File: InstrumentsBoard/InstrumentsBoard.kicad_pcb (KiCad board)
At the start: 2 copper layers, 105.4 x 38.1 mm, 24 parts, among them J1 RJ45_LED_Shielded, Q1 BSS138, Q2 BSS138, U1 Teensy4.1_DEV-16771, U2 OKI

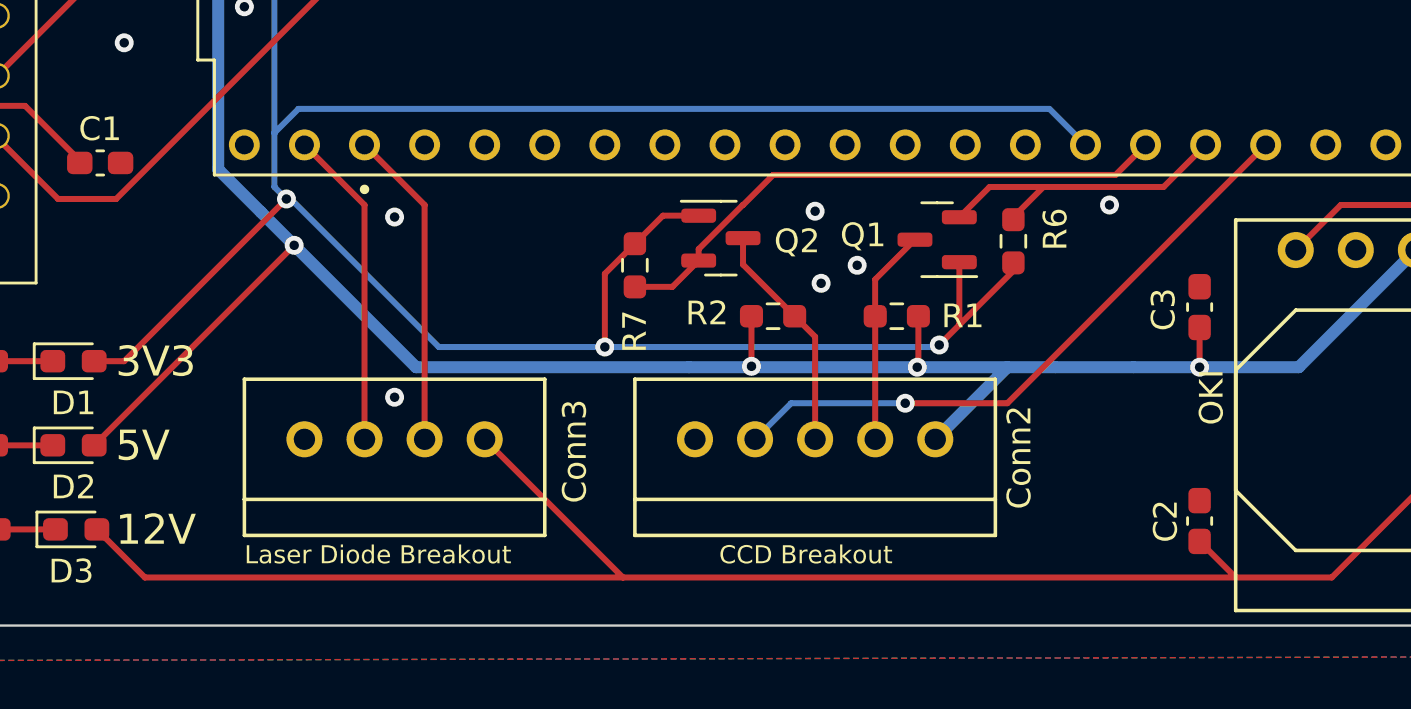
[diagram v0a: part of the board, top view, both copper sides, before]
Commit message: change pin ordering for ccd molex
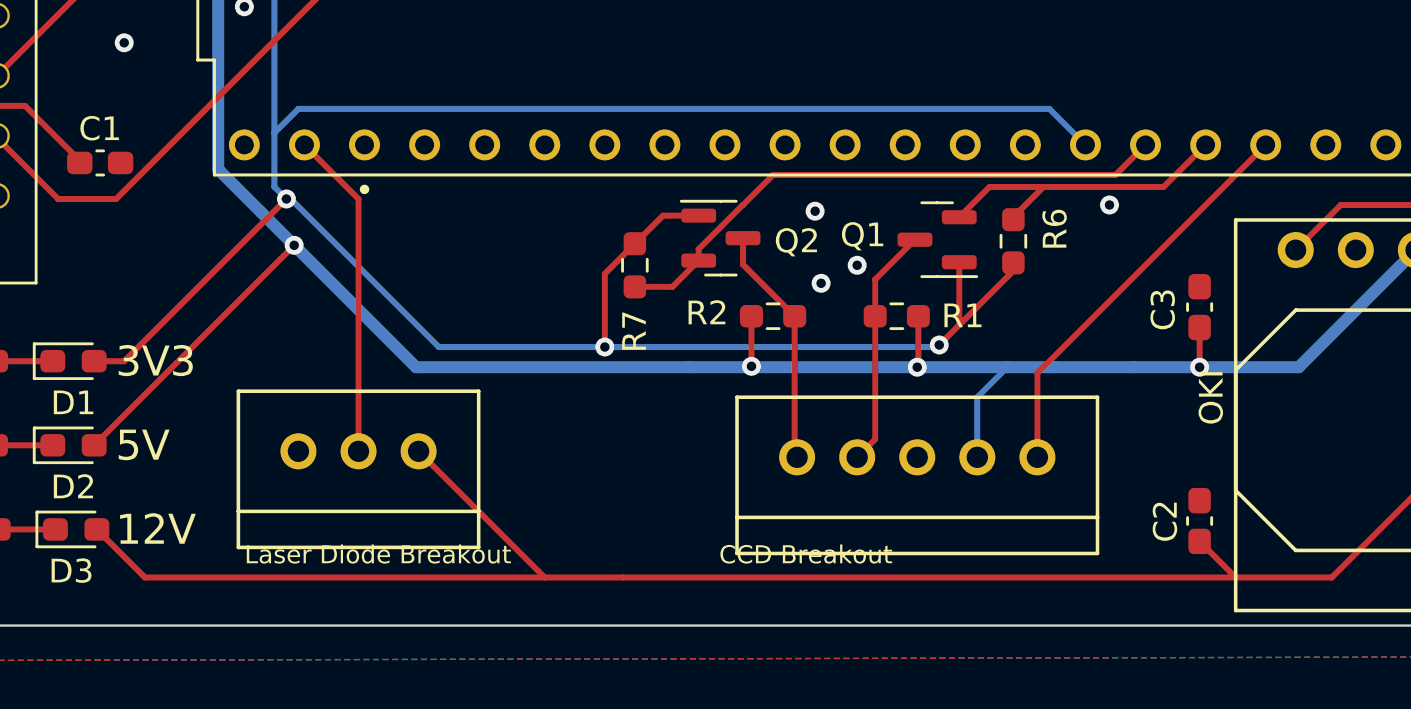
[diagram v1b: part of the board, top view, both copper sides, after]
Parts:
- Conn3: value Molex_SL_04 -> Molex_SL_03; footprint MRDT_Connectors:MOLEX_SL_04_Vertical -> MRDT_Connectors:MOLEX_SL_03_Vertical
- moved Conn2 4.38 mm to (86.4, 66.8)
- moved Conn3 2.84 mm to (60.2, 66.5)
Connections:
- Conn2 pad 1: +5V -> CCD_Vout
- Conn2 pad 2: CCD_CLK_5V -> +5V
- Conn2 pad 3: CCD_ROG_5V -> GND
- Conn2 pad 4: CCD_Vout -> CCD_CLK_5V
- Conn2 pad 5: GND -> CCD_ROG_5V
- Conn3 pad 2: Red_LED -> Green_LED
- Conn3 pad 3: Green_LED -> GND
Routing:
- net Red_LED: track 13.5 -> 0.00 mm
- net CCD_Vout: track 26.7 -> 17.2 mm, vias 1 -> 0
- net CCD_CLK_5V: track 9.14 -> 10.2 mm
- net +12V: track 95.5 -> 94.8 mm
- net GND: vias 9 -> 7

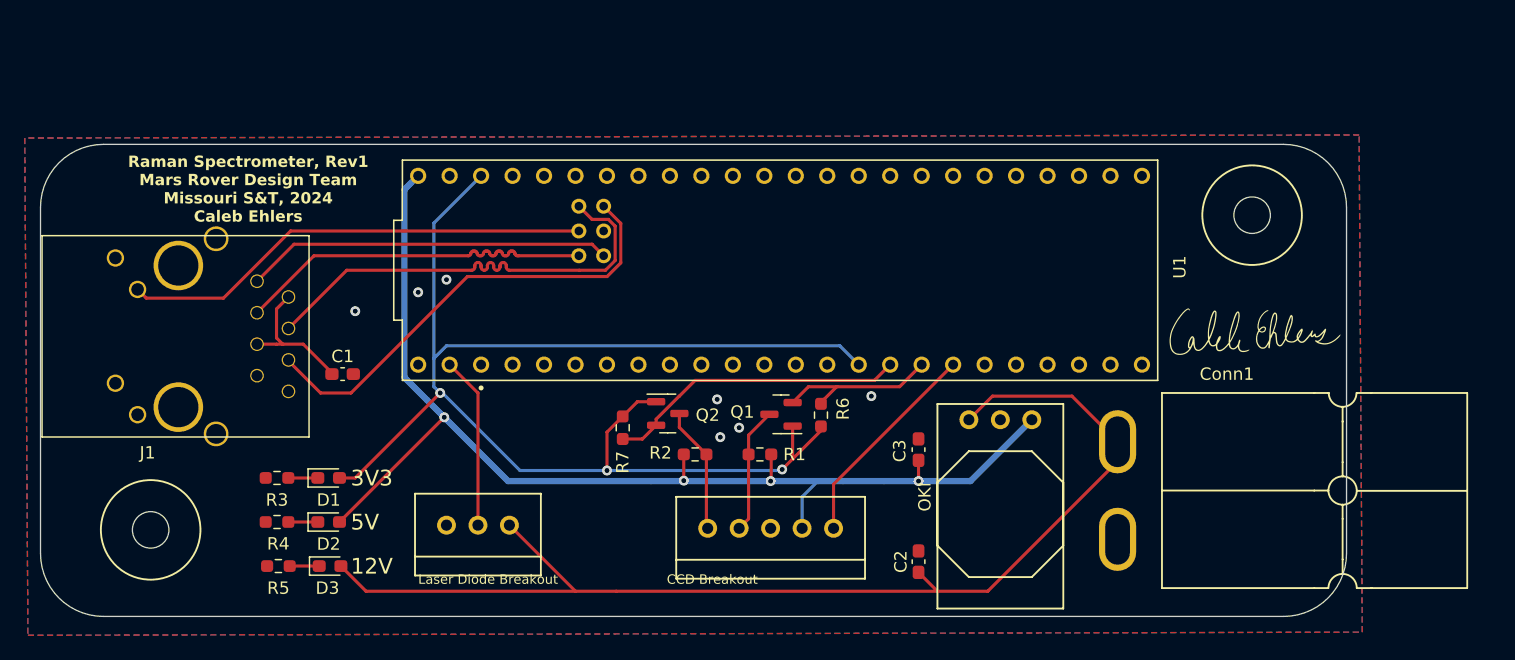
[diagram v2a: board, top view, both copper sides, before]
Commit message: Added Hamamatsu Connector, Updated Silkscreen
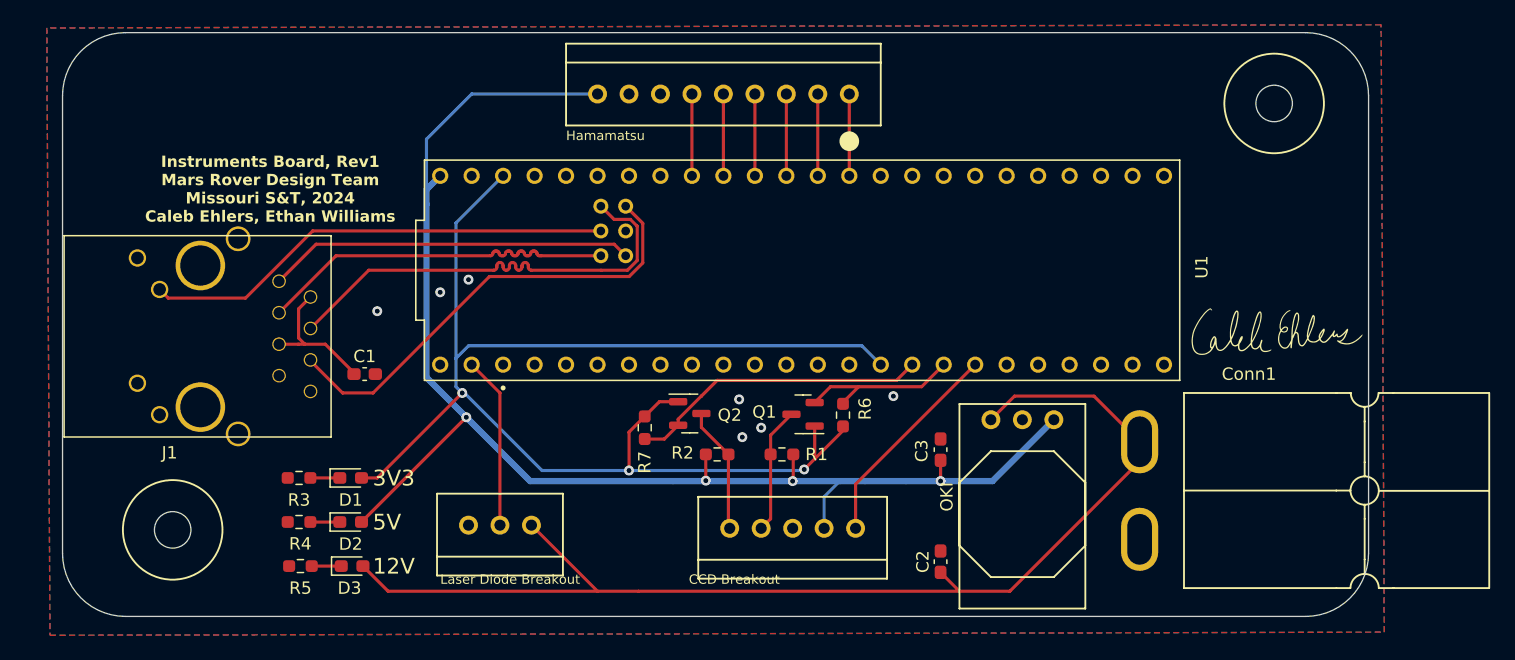
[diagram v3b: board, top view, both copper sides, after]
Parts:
- added Conn4: Molex_SL_09, MRDT_Connectors:MOLEX_SL_09_Vertical, F.Cu at (67.3, 31.8)
- moved V2 9.19 mm to (121.9, 32.5)
- moved C1 1.78 mm to (48.5, 54.4)
- moved Conn2 1.78 mm to (88.1, 66.8)
- moved G*** 1.78 mm to (122.2, 50.8)
- moved R1 1.78 mm to (82.2, 60.8)
- moved R2 1.78 mm to (77.0, 60.8)
- moved R6 1.78 mm to (87.1, 57.7)
- moved R7 1.78 mm to (71.1, 58.7)
- moved U2 1.78 mm to (99.1, 58.0)
- moved V1 1.78 mm to (33.0, 66.9)
- moved Conn3 1.78 mm to (62.0, 66.5)
- moved D1 1.78 mm to (47.4, 62.7)
- moved D2 1.78 mm to (47.4, 66.3)
- moved D3 1.78 mm to (47.5, 69.8)
- moved J1 1.78 mm to (22.3, 51.4)
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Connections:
- U1 pad 13: unconnected-(U1-SCK-Pad13) -> WHITE_LED
- U1 pad 14: unconnected-(U1-A0-Pad14) -> VIDEO
- U1 pad 15: unconnected-(U1-A1-Pad15) -> CLK
- U1 pad 16: unconnected-(U1-A2-Pad16) -> START
- U1 pad 17: unconnected-(U1-A3-Pad17) -> TRG
- U1 pad 18: unconnected-(U1-A4-Pad18) -> EOS
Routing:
- net +5V: track 95.3 -> 115.9 mm
- net WHITE_LED: track 0.00 -> 6.60 mm
- net VIDEO: track 0.00 -> 6.60 mm
- net TRG: track 0.00 -> 6.60 mm
- net START: track 0.00 -> 6.60 mm
- net EOS: track 0.00 -> 6.60 mm
- net CLK: track 0.00 -> 6.60 mm
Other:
- board size 105.4 x 38.1 mm -> 105.4 x 47.1 mm
- board text added: "Hamamatsu"
- board text added: "Instruments Board, Rev1 Mars Rover Design Team Missouri S&T, 2024 Caleb Ehlers, Ethan Williams"
- board text removed: "Raman Spectrometer, Rev1 Mars Rover Design Team Missouri S&T, 2024 Caleb Ehlers"

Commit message: Labeled All Pins, Shifted Teensy Over
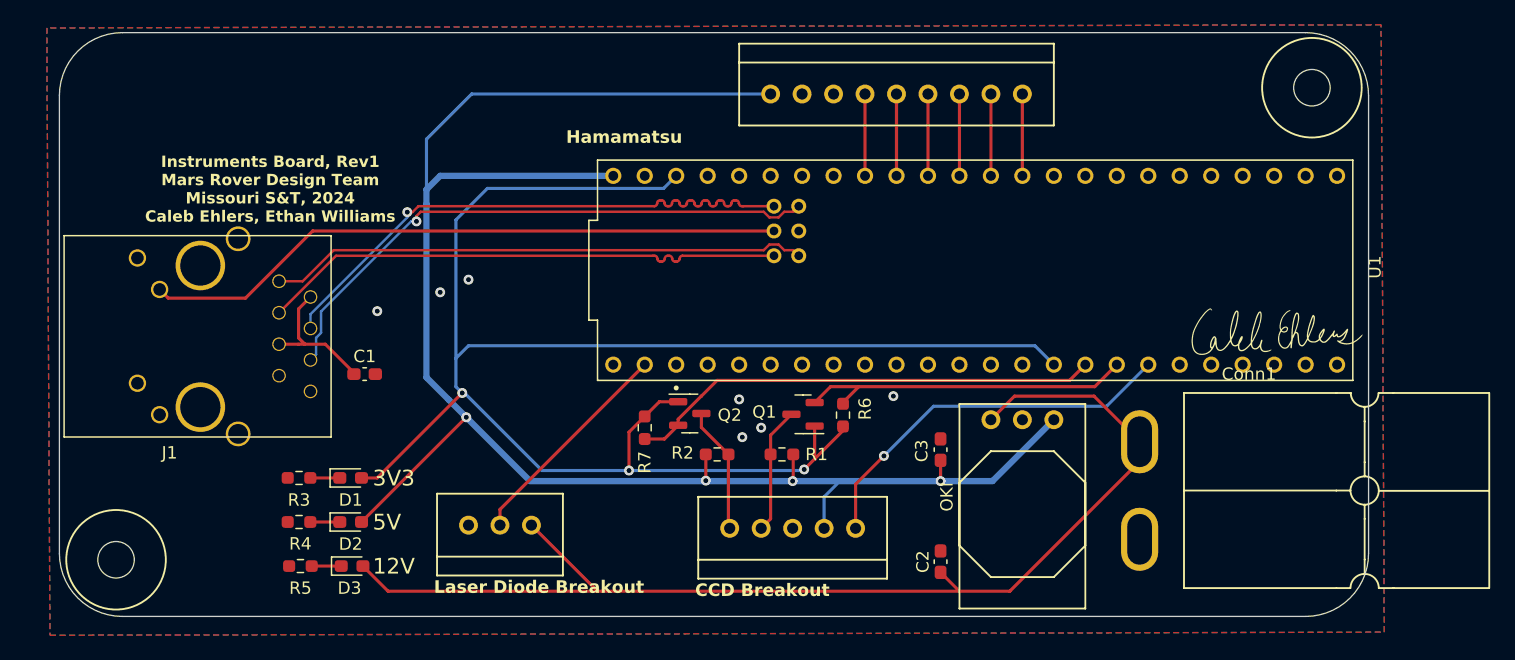
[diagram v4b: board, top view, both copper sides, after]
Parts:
- moved U1 14.0 mm to (97.8, 46.0)
- moved Conn4 14.0 mm to (81.3, 31.8)
- moved V1 5.17 mm to (28.4, 69.3)
- moved V2 3.30 mm to (125.0, 31.2)
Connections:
- U1 pad 1: Red_LED -> unconnected-(U1-TX1-Pad1)
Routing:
- net +3V3: track 111.6 -> 139.7 mm
- net +5V: track 115.9 -> 143.8 mm
- net CCD_ROG_3V3: track 24.4 -> 38.3 mm
- net LED: track 38.2 -> 52.1 mm
- net CCD_CLK_3V3: track 13.6 -> 27.6 mm
- net CCD_Vout: track 17.2 -> 31.2 mm, vias 0 -> 1
- net T+: track 29.6 -> 43.5 mm
- net T-: track 29.5 -> 42.8 mm
- net R-: track 37.5 -> 47.0 mm, vias 0 -> 1
- net R+: track 37.3 -> 45.5 mm, vias 0 -> 1
- net Green_LED: track 13.9 -> 17.8 mm
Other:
- board size 105.4 x 47.1 mm -> 105.7 x 47.1 mm
- board text added: "CLK"
- board text added: "EOS"
- board text added: "GND"
- board text added: "LED"
- board text added: "ROG"
- board text added: "START"
- board text added: "TRG"
- board text added: "VIDEO"
- board text added: "Vout"

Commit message: remove laser diode board, add laser mosfet
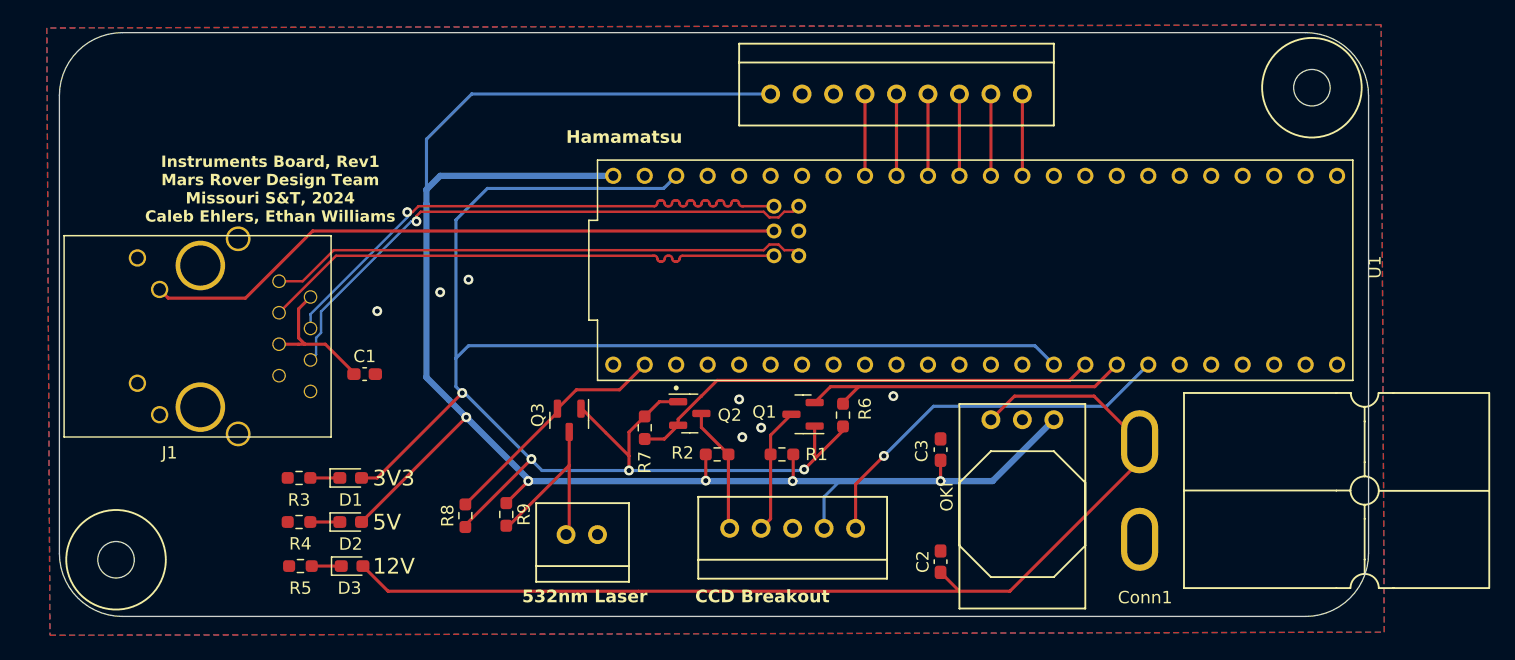
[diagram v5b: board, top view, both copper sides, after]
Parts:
- removed Conn3: Molex_SL_03, MRDT_Connectors:MOLEX_SL_03_Vertical
- removed G***: LOGO, Signatures:Caleb_Ehlers_Signature_15mmx4.8mm
- added Conn5: Molex_SL_02, MRDT_Connectors:MOLEX_SL_02_Vertical, F.Cu at (67.3, 67.3)
- added Q3: BSS138BK, Package_TO_SOT_SMD:SOT-23, F.Cu at (65.0, 58.1)
- added R8: 4.7k, Resistor_SMD:R_0603_1608Metric_Pad0.98x0.95mm_HandSolder, F.Cu at (56.6, 65.8)
- added R9: 4.7k, Resistor_SMD:R_0603_1608Metric_Pad0.98x0.95mm_HandSolder, F.Cu at (59.9, 65.7)
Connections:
- U1 pad 0: Green_LED -> Green_Laser_3V3
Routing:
- net Green_Laser_3V3: track 0.00 -> 19.3 mm
- net Green_LED: track 17.8 -> 0.00 mm
- net Green_Laser_5V: track 0.00 -> 15.5 mm
- net +3V3: track 139.7 -> 152.8 mm, vias 3 -> 4
- net +12V: track 94.8 -> 87.3 mm
- net +5V: track 143.8 -> 146.3 mm, vias 4 -> 5
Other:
- board text added: "532nm Laser"
- board text added: "5V Signal"
- board text removed: "Laser Diode Breakout"
